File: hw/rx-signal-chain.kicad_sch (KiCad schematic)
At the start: 50 parts, among them T301 12t primary : 6T #26 trifilar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, U301 OPA1692xDGK, U302 SN74LVC04APW, U304 AS183-92LF, U305 AS183-92LF, U306 AS183-92LF, U307 AK5578EN

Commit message: I think I have finished the relay conversion and 5V SPI I/O expander crap
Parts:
- renumbered C301 to C7727, C302 to C7728, C303 to C7729, C304 to C7730, C305 to C7731, C306 to C7732, C307 to C7733, C308 to C7734, C309 to C7735, C310 to C7736, C311 to C7737, C312 to C7738, C313 to C7739, C314 to C7740, C315 to C7741, C316 to C7742, C317 to C7743, C318 to C7744, C319 to C7745, C320 to C7746, C321 to C7747, C322 to C7748, C323 to C7749, C324 to C7750, C325 to C7751, C326 to C7752, C327 to C7753, D301 to D7701, FB301 to FB7701, FB302 to FB7702, L301 to L7701, L302 to L7702, R301 to R7707, R302 to R7708, R303 to R7709, R304 to R7710, R305 to R7711, R306 to R7712, R307 to R7713, R308 to R7714, R309 to R7715, R310 to R7716, T301 to T7701, U301 to U7702, U302 to U7703, U303 to U7704, U304 to U7705, U305 to U7706, U306 to U7707, U307 to U7708

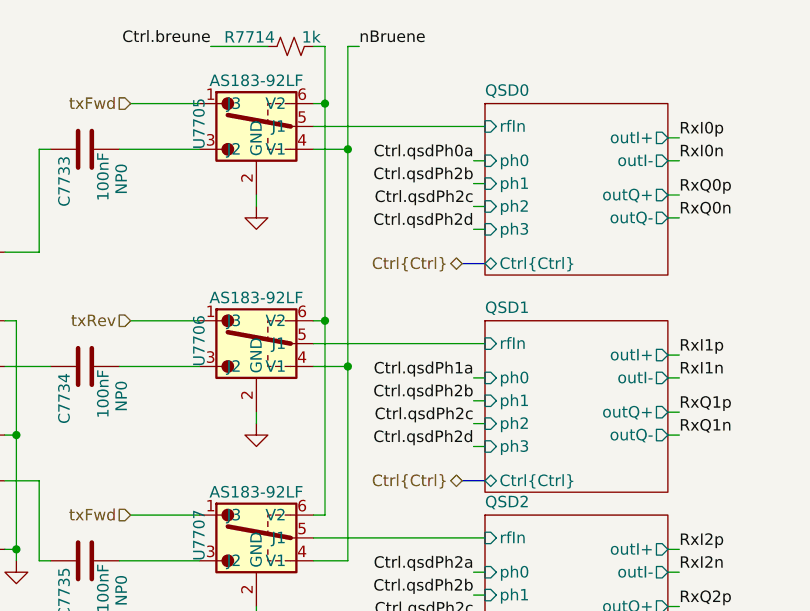
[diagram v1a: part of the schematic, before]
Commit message: Checkpoint. FPGA is mostly done (need a check!). Working on new LPFs. Need inductor footprints and to fix a bunch of broken/missing footprints.
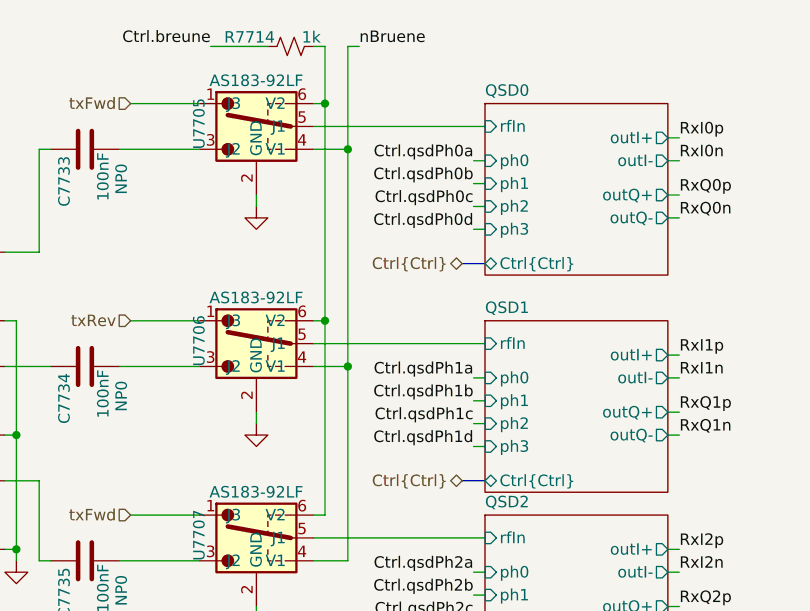
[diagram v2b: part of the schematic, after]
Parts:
- C7727, C7730, C7737, C7739, C7741, C7747, C7748, C7750, C7753: footprint Capacitor_SMD:C_0805_2012Metric -> Capacitor_SMD:C_0603_1608Metric
- R7712, R7713: footprint Resistor_SMD:R_0603_1608Metric -> Resistor_SMD:R_0402_1005Metric
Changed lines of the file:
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@@
 		)
 	)
-	(label "Ctrl.qsdPh2b"
+	(label "Ctrl.qsdPh1b"
 		(at 124.46 138.43 180)
 		(effects
@@
 		)
 	)
-	(label "Ctrl.qsdPh2d"
+	(label "Ctrl.qsdPh1d"
 		(at 124.46 143.51 180)
 		(effects
@@
 		)
 	)
-	(label "Ctrl.qsdPh2d"
+	(label "Ctrl.qsdPh0d"
 		(at 124.46 119.38 180)
 		(effects
@@
 		)
 	)
-	(label "Ctrl.qsdPh2b"
+	(label "Ctrl.qsdPh0b"
 		(at 124.46 114.3 180)
 		(effects
@@
 		)
 	)
-	(label "Ctrl.qsdPh2c"
+	(label "Ctrl.qsdPh0c"
 		(at 124.46 116.84 180)
 		(effects
@@
 		)
 	)
-	(label "Ctrl.qsdPh2c"
+	(label "Ctrl.qsdPh1c"
 		(at 124.46 140.97 180)
 		(effects
@@
 			)
 		)
-		(property "Footprint" "Resistor_SMD:R_0603_1608Metric"
+		(property "Footprint" "Resistor_SMD:R_0402_1005Metric"
 			(at 74.676 73.914 90)
 			(effects
@@
 			)
 		)
-		(property "Footprint" "Capacitor_SMD:C_0805_2012Metric"
+		(property "Footprint" "Capacitor_SMD:C_0603_1608Metric"
 			(at 260.0452 161.29 0)
 			(effects
@@
 			)
 		)
-		(property "Footprint" "Capacitor_SMD:C_0805_2012Metric"
+		(property "Footprint" "Capacitor_SMD:C_0603_1608Metric"
 			(at 200.3552 153.67 0)
 			(effects
@@
 			)
 		)
-		(property "Footprint" "Capacitor_SMD:C_0805_2012Metric"
+		(property "Footprint" "Capacitor_SMD:C_0603_1608Metric"
 			(at 50.4952 196.85 0)
 			(effects
@@
 			)
 		)
-		(property "Footprint" "Capacitor_SMD:C_0805_2012Metric"
+		(property "Footprint" "Capacitor_SMD:C_0603_1608Metric"
 			(at 119.6848 193.04 0)
 			(effects
@@
 			)
 		)
-		(property "Footprint" "Resistor_SMD:R_0603_1608Metric"
+		(property "Footprint" "Resistor_SMD:R_0402_1005Metric"
 			(at 74.676 44.704 90)
 			(effects
@@
 			)
 		)
-		(property "Footprint" "Capacitor_SMD:C_0805_2012Metric"
+		(property "Footprint" "Capacitor_SMD:C_0603_1608Metric"
 			(at 103.1748 193.04 0)
 			(effects
@@
 			)
 		)
-		(property "Footprint" "Capacitor_SMD:C_0805_2012Metric"
+		(property "Footprint" "Capacitor_SMD:C_0603_1608Metric"
 			(at 152.7048 193.04 0)
 			(effects
@@
 			)
 		)
-		(property "Footprint" "Capacitor_SMD:C_0805_2012Metric"
+		(property "Footprint" "Capacitor_SMD:C_0603_1608Metric"
 			(at 136.1948 193.04 0)
 			(effects
@@
 			)
 		)
-		(property "Footprint" "Capacitor_SMD:C_0805_2012Metric"
+		(property "Footprint" "Capacitor_SMD:C_0603_1608Metric"
 			(at 221.9452 157.48 0)
 			(effects
@@
 			)
 		)
-		(property "Footprint" "Capacitor_SMD:C_0805_2012Metric"
+		(property "Footprint" "Capacitor_SMD:C_0603_1608Metric"
 			(at 19.3548 193.04 0)
 			(effects

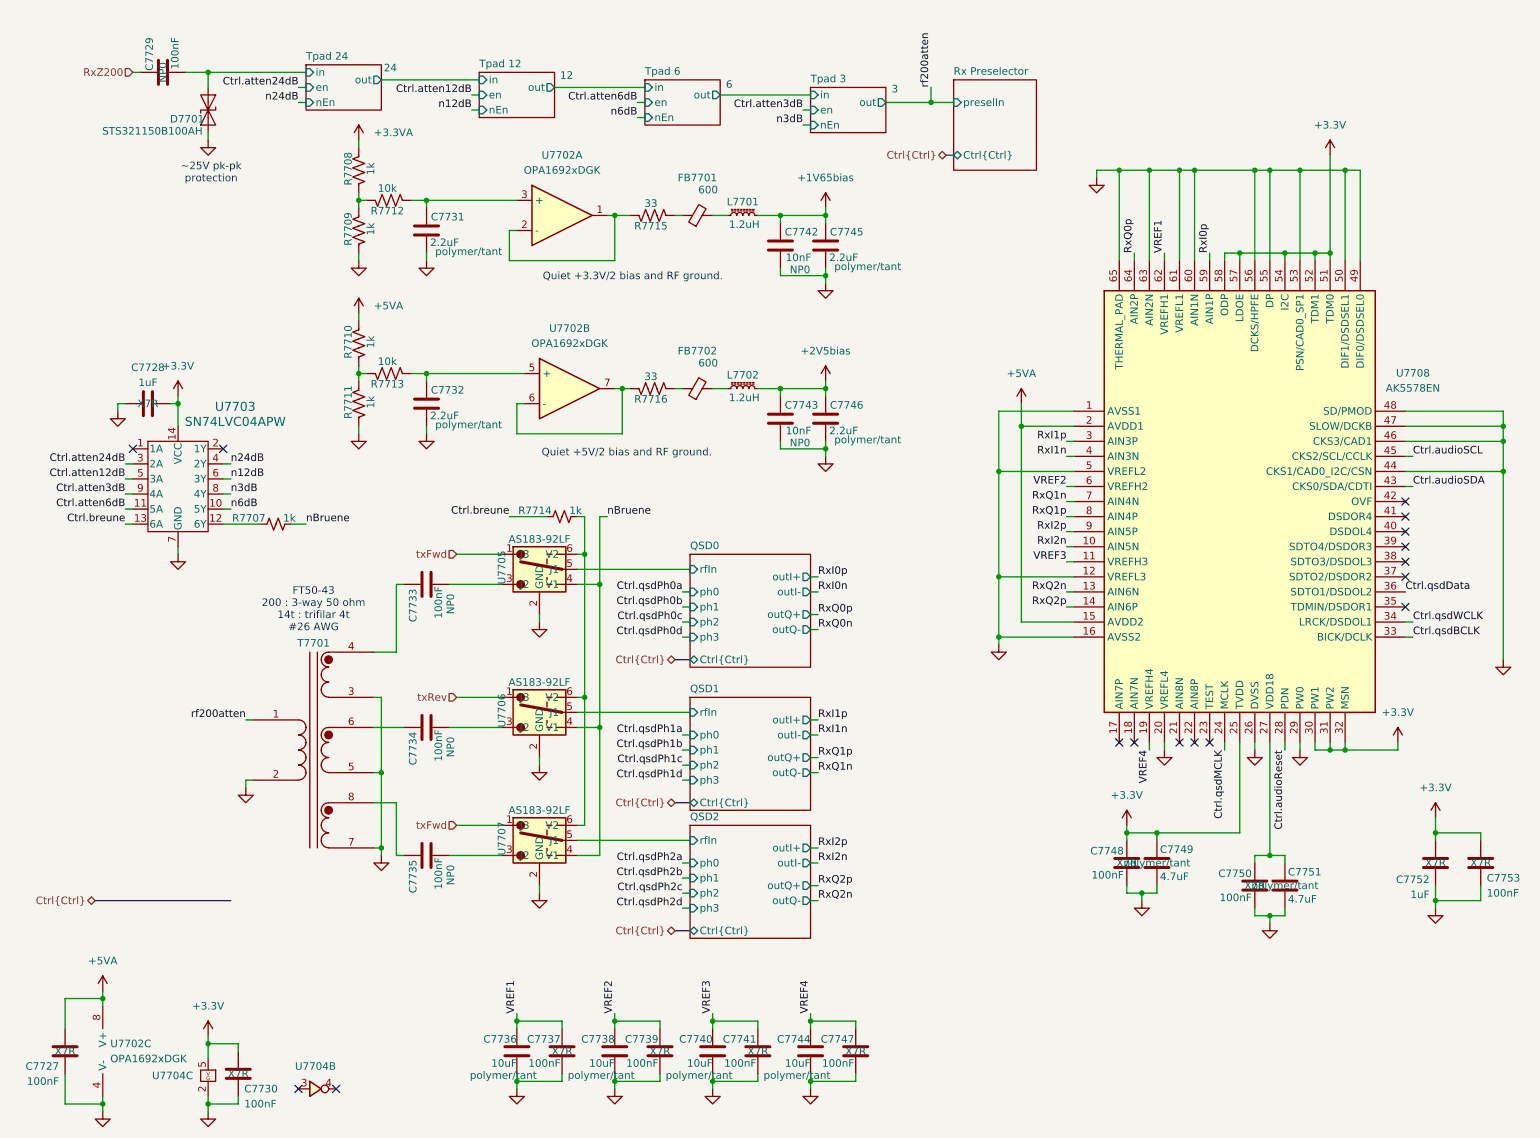
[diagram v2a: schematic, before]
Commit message: OK I have part numbers for consolidated caps, resistors, inductors and all ICs are now Uxxx refdes.
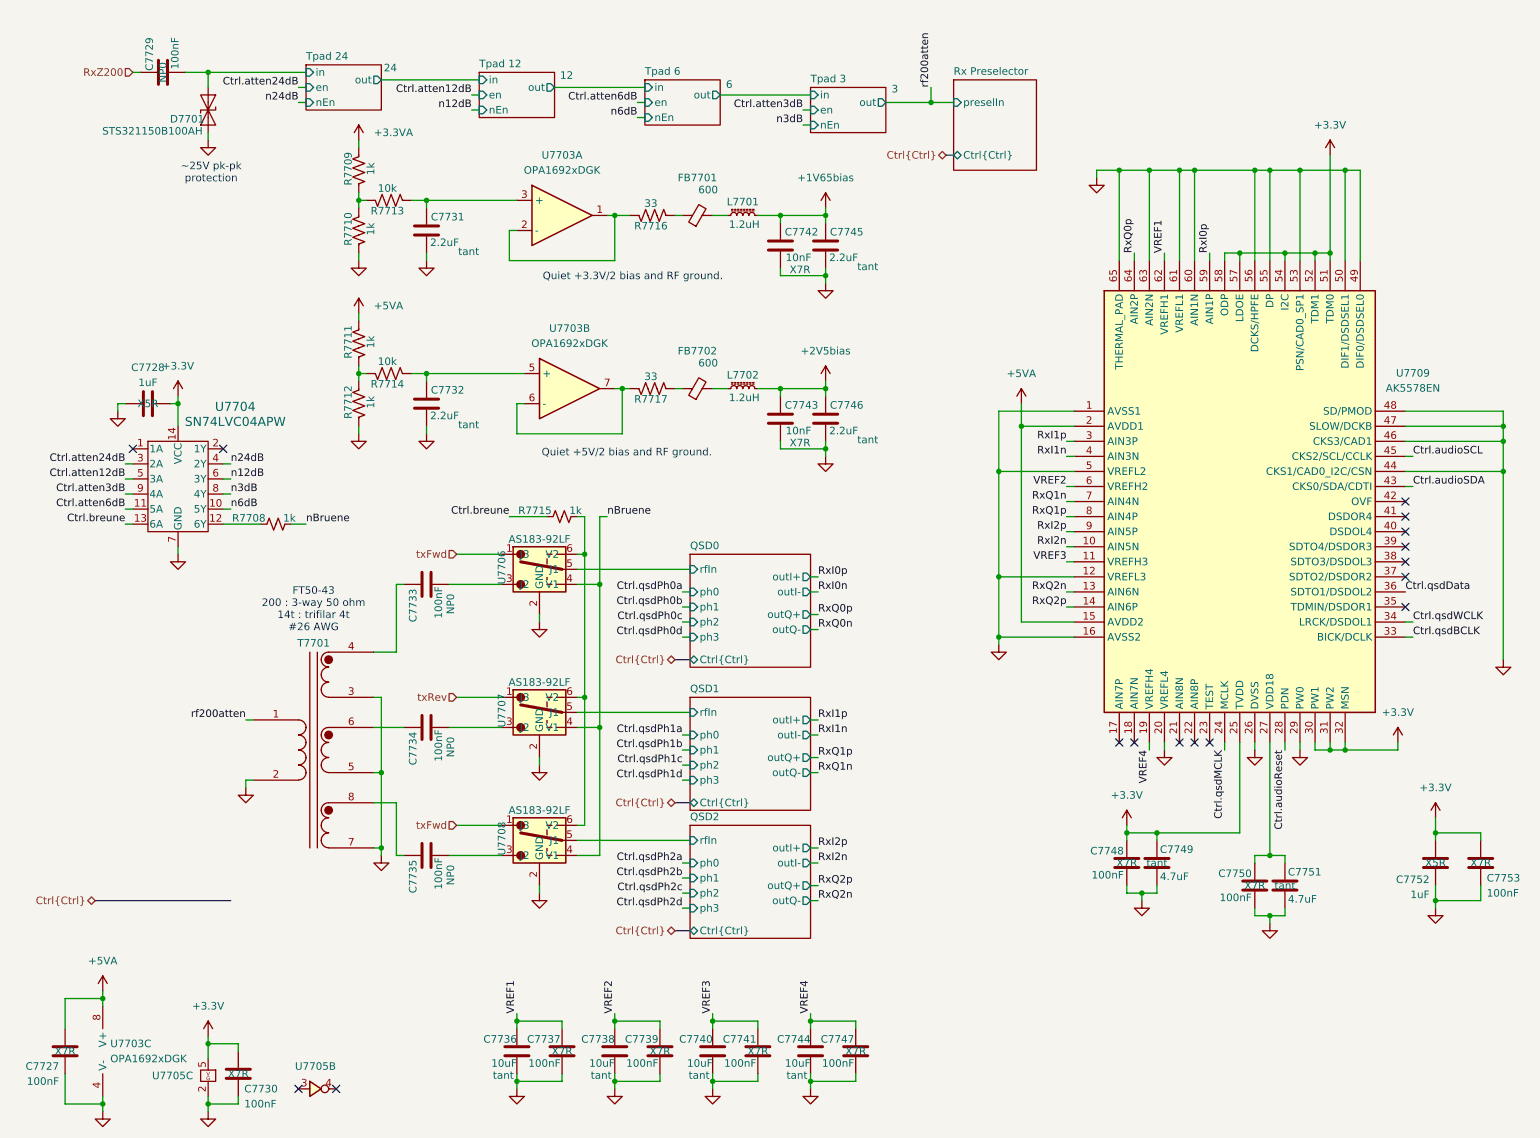
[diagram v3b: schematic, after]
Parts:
- C7728, C7752: footprint Capacitor_SMD:C_0603_1608Metric -> Capacitor_SMD:C_0402_1005Metric; Manufacturer_Name TDK -> Murata; Manufacturer_Part_Number C1608X7R1H105K080AB -> GRM155R61E105KE11D; Mouser Part Number 810-C1608X7R1H105K08 -> 81-GRM155R61E105KE1D; cap-type X7R -> X5R; working-voltage 50V -> 25V
- C7729, C7733, C7734, C7735: working-voltage 100V -> 50V
- C7731, C7732, C7745, C7746: cap-type polymer/tant -> tant
- C7736, C7738, C7740, C7744: Manufacturer_Part_Number TLCR106M020RTA -> TAJD106K050RNJ; Mouser Part Number 581-TLCR106M020RTA -> 581-TAJD106K050R; cap-type polymer/tant -> tant; working-voltage 20V -> 50V
- C7742, C7743: cap-type NP0 -> X7R
- C7749, C7751: Manufacturer_Name Kyocera AVX -> Vishay/Sprague; Manufacturer_Part_Number TPCR475K020R2000 -> 298D475X9010M2T; Mouser Part Number 581-TPCR475K020R2000 -> 74-298D475X9010M2T; cap-type polymer/tant -> tant
- renumbered R7707 to R7708, R7708 to R7709, R7709 to R7710, R7710 to R7711, R7711 to R7712, R7712 to R7713, R7713 to R7714, R7714 to R7715, R7715 to R7716, R7716 to R7717, U7702 to U7703, U7703 to U7704, U7704 to U7705, U7705 to U7706, U7706 to U7707, U7707 to U7708, U7708 to U7709

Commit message: Checkpoint for yet another merge
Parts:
- removed C7730: 100nF, Capacitor_SMD:C_0603_1608Metric, symbol Device:C
- removed U7705: ~, Library:SOT65P220X110-6N, symbol Library:74LVC2G04
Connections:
- no-connect marks 16 -> 14
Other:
- note added: "Quiet +3.3VA/2 bias and RF ground."
- note added: "Quiet +5VA/2 bias and RF ground."
- note removed: "Quiet +3.3V/2 bias and RF ground."
- note removed: "Quiet +5V/2 bias and RF ground."

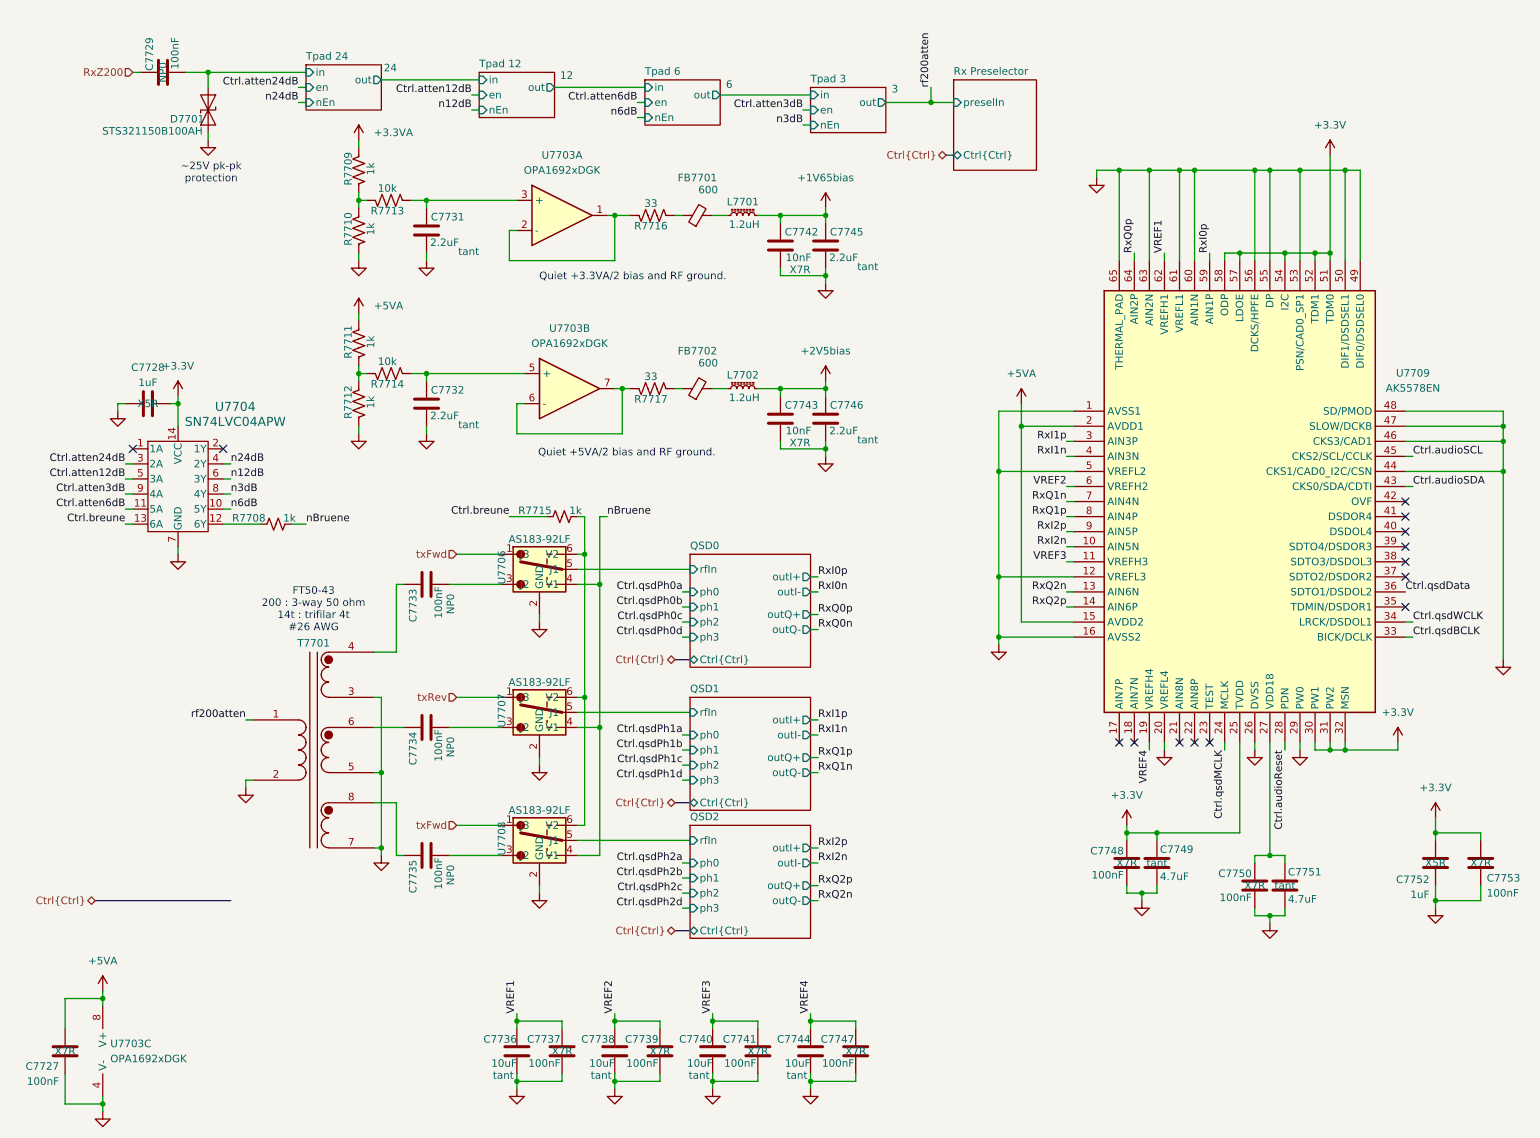
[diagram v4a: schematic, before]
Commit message: All symbols and footprints seem right now, and schematic again imports into PCB without error
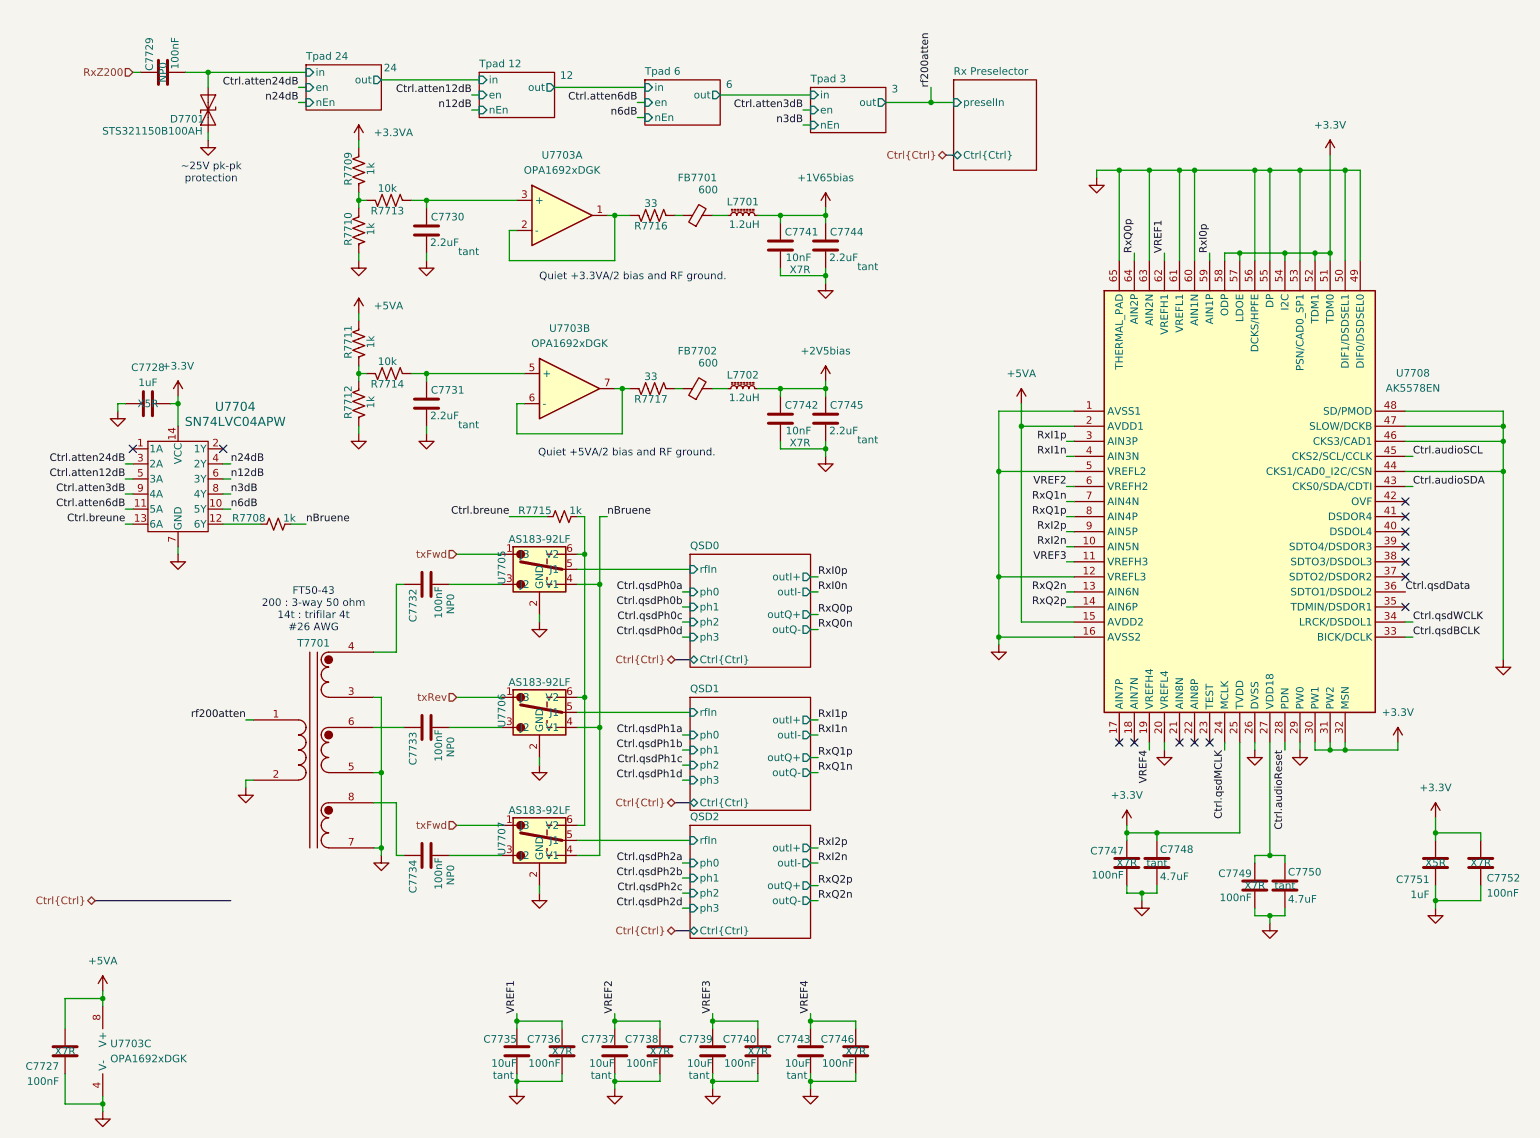
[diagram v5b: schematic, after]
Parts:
- renumbered C7731 to C7730, C7732 to C7731, C7733 to C7732, C7734 to C7733, C7735 to C7734, C7736 to C7735, C7737 to C7736, C7738 to C7737, C7739 to C7738, C7740 to C7739, C7741 to C7740, C7742 to C7741, C7743 to C7742, C7744 to C7743, C7745 to C7744, C7746 to C7745, C7747 to C7746, C7748 to C7747, C7749 to C7748, C7750 to C7749, C7751 to C7750, C7752 to C7751, C7753 to C7752, U7706 to U7705, U7707 to U7706, U7708 to U7707, U7709 to U7708

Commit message: Off to a great start building just the NexRx
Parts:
- removed C7729: 100nF, Capacitor_SMD:C_1206_3216Metric, symbol Device:C
- removed D7701: STS321150B100AH, Diode_SMD:Infineon_SG-WLL-2-3_0.58x0.28_P0.36mm, symbol Diode:ESD131-B1-W0201
- removed R7708, R7715: 1k, Resistor_SMD:R_0402_1005Metric, symbol Device:R_Small_US
- removed U7705, U7706, U7707: AS183-92LF, SOT65P220X110-6N, symbol Library:AS183-92LF
- T301: renamed from T7701; value 12t primary : 6T #26 trifilar secondary FT37-43 -> BN-43-202, 200 : 3-way 50 ohm, pentafilar 2 turns #30 AWG; footprint Library:Toroid-1pri-3sec-ft50 -> Library:Transformer-2P-3S-BN-43-202; symbol Library:Transformer_3S -> Library:Transformer-2P-3S; Core (none) -> Amidon BN-43-202
- renumbered C7727 to C301, C7728 to C302, C7730 to C303, C7731 to C304, C7732 to C305, C7733 to C306, C7734 to C307, C7735 to C308, C7736 to C309, C7737 to C310, C7738 to C311, C7739 to C312, C7740 to C313, C7741 to C314, C7742 to C315, C7743 to C316, C7744 to C317, C7745 to C318, C7746 to C319, C7747 to C320, C7748 to C321, C7749 to C322, C7750 to C323, C7751 to C324, C7752 to C325, FB7701 to FB301, FB7702 to FB302, L7701 to L301, L7702 to L302, R7709 to R301, R7710 to R302, R7711 to R303, R7712 to R304, R7713 to R305, R7714 to R306, R7716 to R307, R7717 to R308, U7703 to U301, U7704 to U302, U7708 to U303
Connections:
- net GND: now also T301.10 (OUT2B), T301.4 (IN2-), T301.6 (OUT1B), T301.8 (OUT2B); no longer T301.2 (IN-), T301.3 (OUT1B), T301.5 (OUT2B), T301.7 (OUT2B)
- net QSD0/rfIn: now also C305.2
- net QSD1/rfIn: now also C306.2
- net QSD2/rfIn: now also C307.2
- net at C307.1: now also T301.9 (OUT2A); no longer T301.8 (OUT2A)
- net at C306.1: now also T301.7 (OUT2A); no longer T301.6 (OUT2A)
- net at C305.1: now also T301.5 (OUT1A); no longer T301.4 (OUT1A)
- net Ctrl.breune: no longer names the net of U302.13 (6A)
- new net: T301.2 (IN1-), T301.3 (IN2+)
- no-connect marks 14 -> 16
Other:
- note added: "BN-43-202 200 : 3-way 50 ohm pentafilar 2 turns #30 AWG"
- note removed: "FT50-43 200 : 3-way 50 ohm 14t : trifilar 4t #26 AWG"
- note removed: "~25V pk-pk protection"
- moved on the sheet: C305, C306, C307
